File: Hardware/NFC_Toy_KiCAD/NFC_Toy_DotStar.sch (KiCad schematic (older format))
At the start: 29 parts, among them J20 TP, J21 TP, U10 APA102, U11 APA102, U12 SN74LVC2T45, U13 APA102, U14 APA102, U15 APA102, U16 APA102, U17 APA102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

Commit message: Layout started
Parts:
- removed J20, J21: TP, symbol TEST_1P
- added TP14, TP15: TEST, NFC_Toy_Lib:Test_Point, symbol TEST
- C35, C36, C37, C38, C39, C40, C41, C42, C43, C44, C45, C46, C47, C48: footprint (none) -> Capacitors_SMD:C_0402
- U10, U11, U13, U14, U15, U16, U17, U18, U6, U7, U8, U9: footprint MODULE -> NFC_Toy_Lib:APA102_hand_solder
- U12: footprint SOP50P310X90-8N -> NFC_Toy_Lib:SOP50P310X90-8N

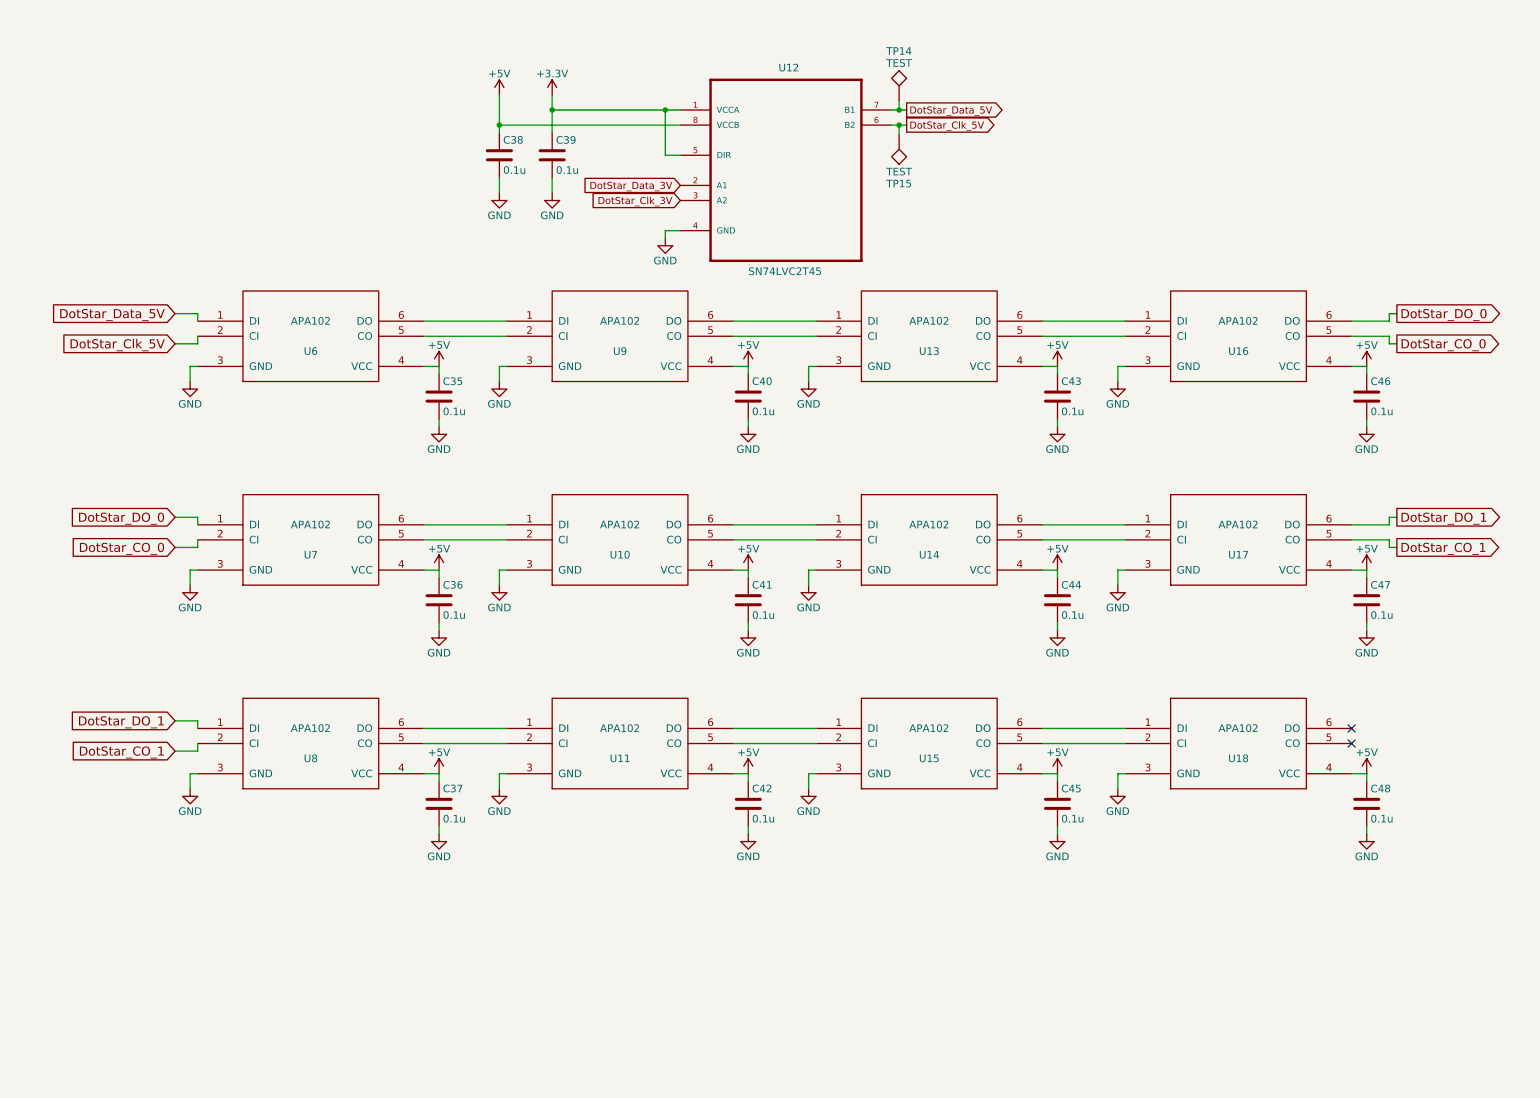
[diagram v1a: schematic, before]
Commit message: Component placement complete.
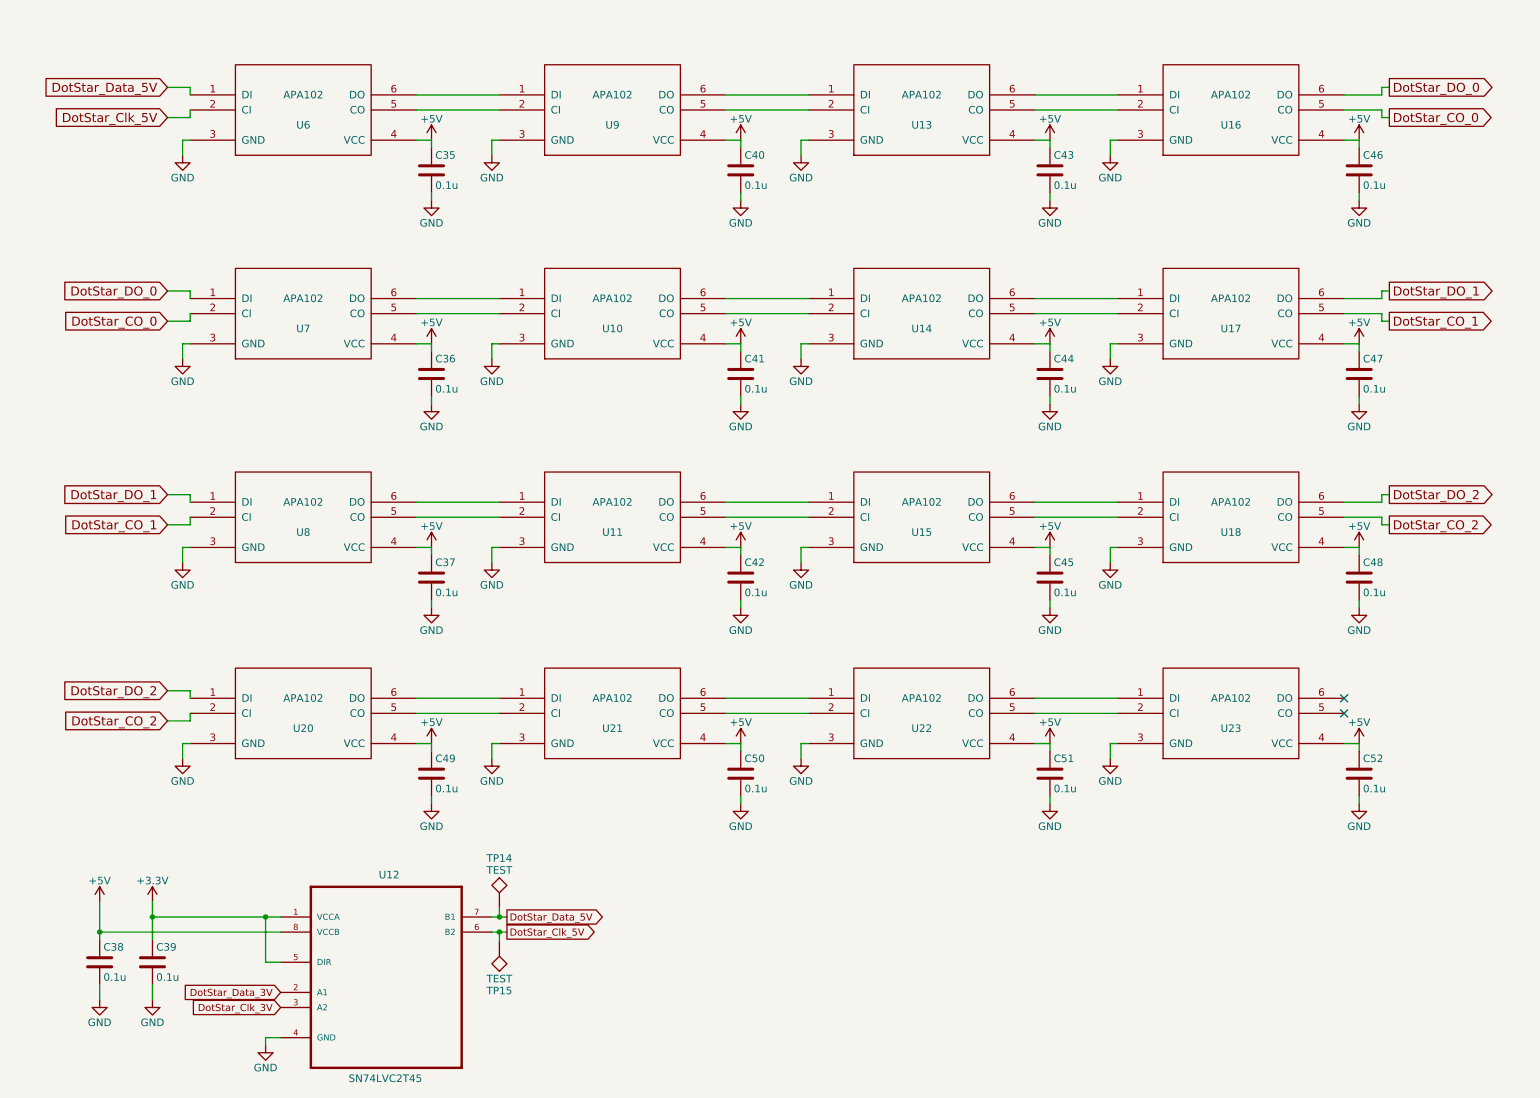
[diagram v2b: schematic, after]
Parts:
- added C49, C50, C51, C52: 0.1u, Capacitors_SMD:C_0402, symbol C
- added U20, U21, U22, U23: APA102, NFC_Toy_Lib:APA102_hand_solder, symbol APA102
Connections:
- net +5V: now also C49.1, C50.1, C51.1, C52.1, U20.4 (VCC), U21.4 (VCC), U22.4 (VCC), U23.4 (VCC)
- net GND: now also C49.2, C50.2, C51.2, C52.2, U20.3 (GND), U21.3 (GND), U22.3 (GND), U23.3 (GND)
- net DotStar_CO_2: now reaches U18.5 (CO)
- net DotStar_CO_2: now also U20.2 (CI)
- net DotStar_DO_2: now reaches U18.6 (DO)
- net DotStar_DO_2: now also U20.1 (DI)
- new net: U20.5 (CO), U21.2 (CI)
- new net: U20.6 (DO), U21.1 (DI)
- new net: U21.5 (CO), U22.2 (CI)
- new net: U21.6 (DO), U22.1 (DI)
- new net: U22.5 (CO), U23.2 (CI)
- new net: U22.6 (DO), U23.1 (DI)
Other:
- moved on the sheet: C35, C36, C37, C38, C39, C40, C41, C42, C43, C44, C45, C46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

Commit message: Added RNG and "Try Again"
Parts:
- C?: renamed from C35; symbol C -> Device:C
- C?: renamed from C40; symbol C -> Device:C
- C?: renamed from C43; symbol C -> Device:C
- C?: renamed from C46; symbol C -> Device:C
- C?: renamed from C36; symbol C -> Device:C
- C?: renamed from C41; symbol C -> Device:C
- C?: renamed from C44; symbol C -> Device:C
- C?: renamed from C47; symbol C -> Device:C
- C?: renamed from C37; symbol C -> Device:C
- C?: renamed from C42; symbol C -> Device:C
- C?: renamed from C45; symbol C -> Device:C
- C?: renamed from C48; symbol C -> Device:C
- C?: renamed from C38; symbol C -> Device:C
- C?: renamed from C39; symbol C -> Device:C
- C?: renamed from C49; symbol C -> Device:C
- C?: renamed from C50; symbol C -> Device:C
- C?: renamed from C51; symbol C -> Device:C
- C?: renamed from C52; symbol C -> Device:C
- TP?: renamed from TP14; symbol TEST -> NFC_Toy-rescue:TEST
- TP?: renamed from TP15; symbol TEST -> NFC_Toy-rescue:TEST
- U?: renamed from U6; symbol APA102 -> APA102:APA102
- U?: renamed from U9; symbol APA102 -> APA102:APA102
- U?: renamed from U13; symbol APA102 -> APA102:APA102
- U?: renamed from U16; symbol APA102 -> APA102:APA102
- U?: renamed from U7; symbol APA102 -> APA102:APA102
- U?: renamed from U10; symbol APA102 -> APA102:APA102
- U?: renamed from U14; symbol APA102 -> APA102:APA102
- U?: renamed from U17; symbol APA102 -> APA102:APA102
- U?: renamed from U8; symbol APA102 -> APA102:APA102
- U?: renamed from U11; symbol APA102 -> APA102:APA102
- U?: renamed from U15; symbol APA102 -> APA102:APA102
- U?: renamed from U18; symbol APA102 -> APA102:APA102
- U?: renamed from U12; symbol SN74LVC2T45 -> SN74LVC2T45:SN74LVC2T45
- U?: renamed from U20; symbol APA102 -> APA102:APA102
- U?: renamed from U21; symbol APA102 -> APA102:APA102
- U?: renamed from U22; symbol APA102 -> APA102:APA102
- U?: renamed from U23; symbol APA102 -> APA102:APA102
